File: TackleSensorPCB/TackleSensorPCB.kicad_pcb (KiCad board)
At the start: 2 copper layers, 60 x 25 mm, 26 parts, among them J1 PJ-037A, J2 Conn_01x03_Male, J3 Conn_01x04_Male, J4 Conn_01x07_Male, Q1 2N7002, Q2 2N7002, SW1 SW_DPST_x2, U1 TPS62172DSG, U2 MSP430FR2433IRGER, U3 MMA8452QR1

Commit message: Updates
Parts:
- renumbered SW1 to Test

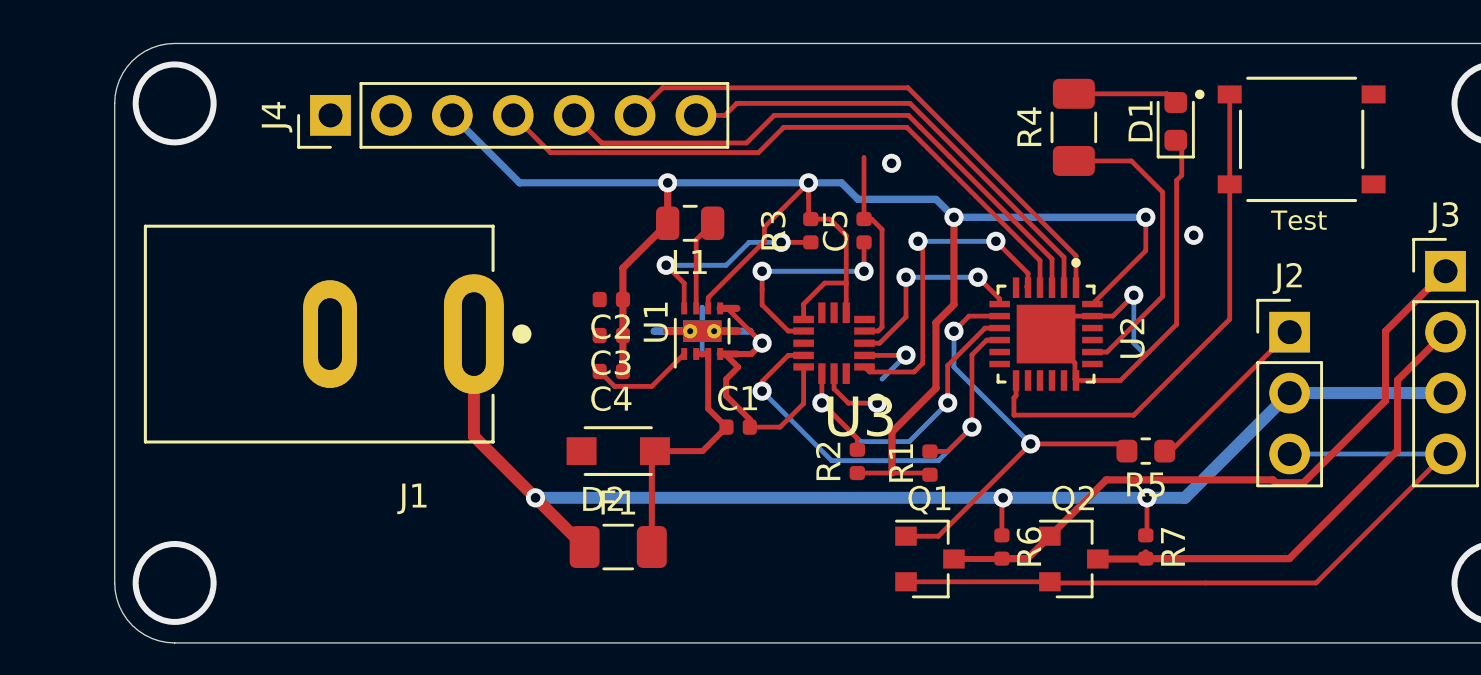
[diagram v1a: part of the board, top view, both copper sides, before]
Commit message: Updated to LS2
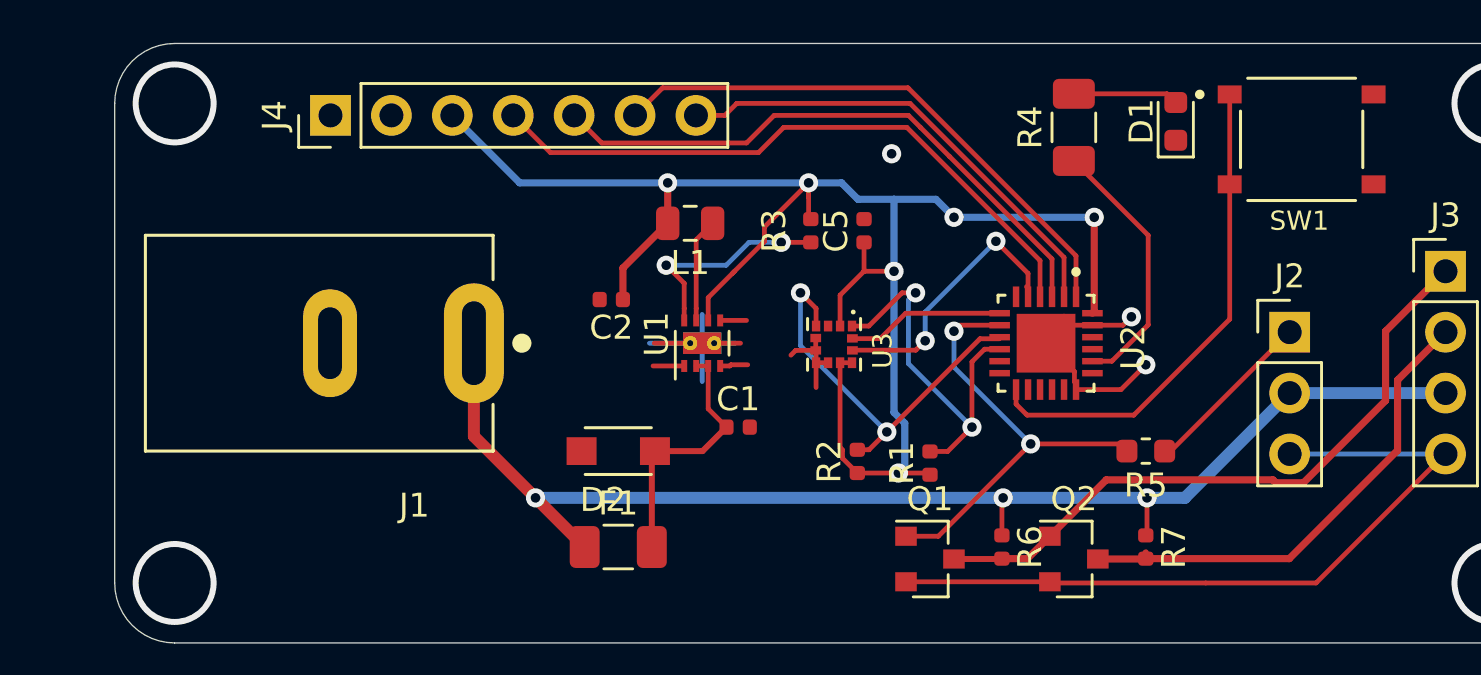
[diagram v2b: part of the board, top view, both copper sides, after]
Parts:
- removed C3, C4: 10uF, Capacitor_SMD:C_0402_1005Metric
- C2: value 10uF -> 47uF
- U3: value MMA8452QR1 -> LIS2DH12TR; footprint MMA8452QR1:QFN50P300X300X100-16N -> LIS2DH12TR:PQFN50P200X200100-12N
- moved U1 0.50 mm to (103.5, 71.5)
- moved J1 0.38 mm to (94.0, 71.5)
- moved U2 0.38 mm to (117.8, 71.5)
- turned U3 to 270 degrees
- renumbered Test to SW1
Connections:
- C5 pad 1: Net-(C5-Pad1) -> +3V3
- U3 pad 1: +3V3 -> SCL
- U3 pad 10: GND -> +3V3
- U3 pad 11: INT1 -> INT2
- U3 pad 12: GND -> INT1
- U3 pad 2: Net-(C5-Pad1) -> +3V3
- U3 pad 3: Net-(U3-Pad3) -> GND
- U3 pad 4: SCL -> SDA
- U3 pad 6: SDA -> GND
- U3 pad 8: Net-(U3-Pad8) -> GND
- U3 pad 9: INT2 -> +3V3
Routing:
- net GND: track 98.1 -> 60.2 mm, vias 10 -> 7
- net Net-(C5-Pad1): track 9.04 -> 0.00 mm, vias 2 -> 0
- net SCL: track 19.7 -> 16.3 mm
- net INT2: track 13.7 -> 11.1 mm
- net SDA: track 14.7 -> 16.9 mm
- net +3V3: track 75.5 -> 73.7 mm, vias 4 -> 6
- net INT1: track 8.33 -> 6.58 mm, vias 2 -> 0
- net L0: track 12.5 -> 11.1 mm
- net SW0: track 21.5 -> 20.7 mm
- net PG: track 8.54 -> 9.04 mm
- net Net-(L1-Pad1): track 3.83 -> 4.33 mm
- net Net-(C1-Pad1): track 11.3 -> 10.8 mm

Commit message: Completed 3D model
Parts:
- SW1: value SW_DPST_x2 -> FSM4JSMA; footprint TS-1187A-B-A-B:SW_TS-1187A-B-A-B -> FSM4JSMA:TE_FSM4JSMA
- moved D1 5.73 mm to (124.8, 67.8), turned to 180 degrees
- moved R4 0.85 mm to (118.2, 62.2)
- moved SW1 0.22 mm to (128.6, 62.8), turned to 180 degrees
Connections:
- SW1 pad 2: GND -> SW0
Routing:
- net SW0: track 20.7 -> 28.2 mm
- net Net-(D1-Pad2): track 4.40 -> 9.89 mm
- net L0: track 11.1 -> 11.8 mm
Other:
- board text added: "3.3V to 17V"
- board text added: "GND"
- board text added: "Programming"
- board text added: "RX"
- board text added: "S0_3V3"
- board text added: "S0_Vin"
- board text added: "TX"
- board text added: "Test"
- board text added: "Vin"
- board text added: "not_S0 Vin"

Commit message: Updated BOM
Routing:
- net GND: track 60.2 -> 62.6 mm
